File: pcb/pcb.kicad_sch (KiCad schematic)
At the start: 57 parts, among them IC1 TPS63802DLAT, IC2 TUSB320LIRWBR, J1 USB_C_Receptacle_PowerOnly_6P, J2 Soil_Sensor, J3 Pump, J4 Conn_01x03, Q1 2N7002, Q2 AO3401A, Q3 AO3400A, U1 BQ24075RGTR, U2 ESP-32S_USB-C_CH340_DevBoard

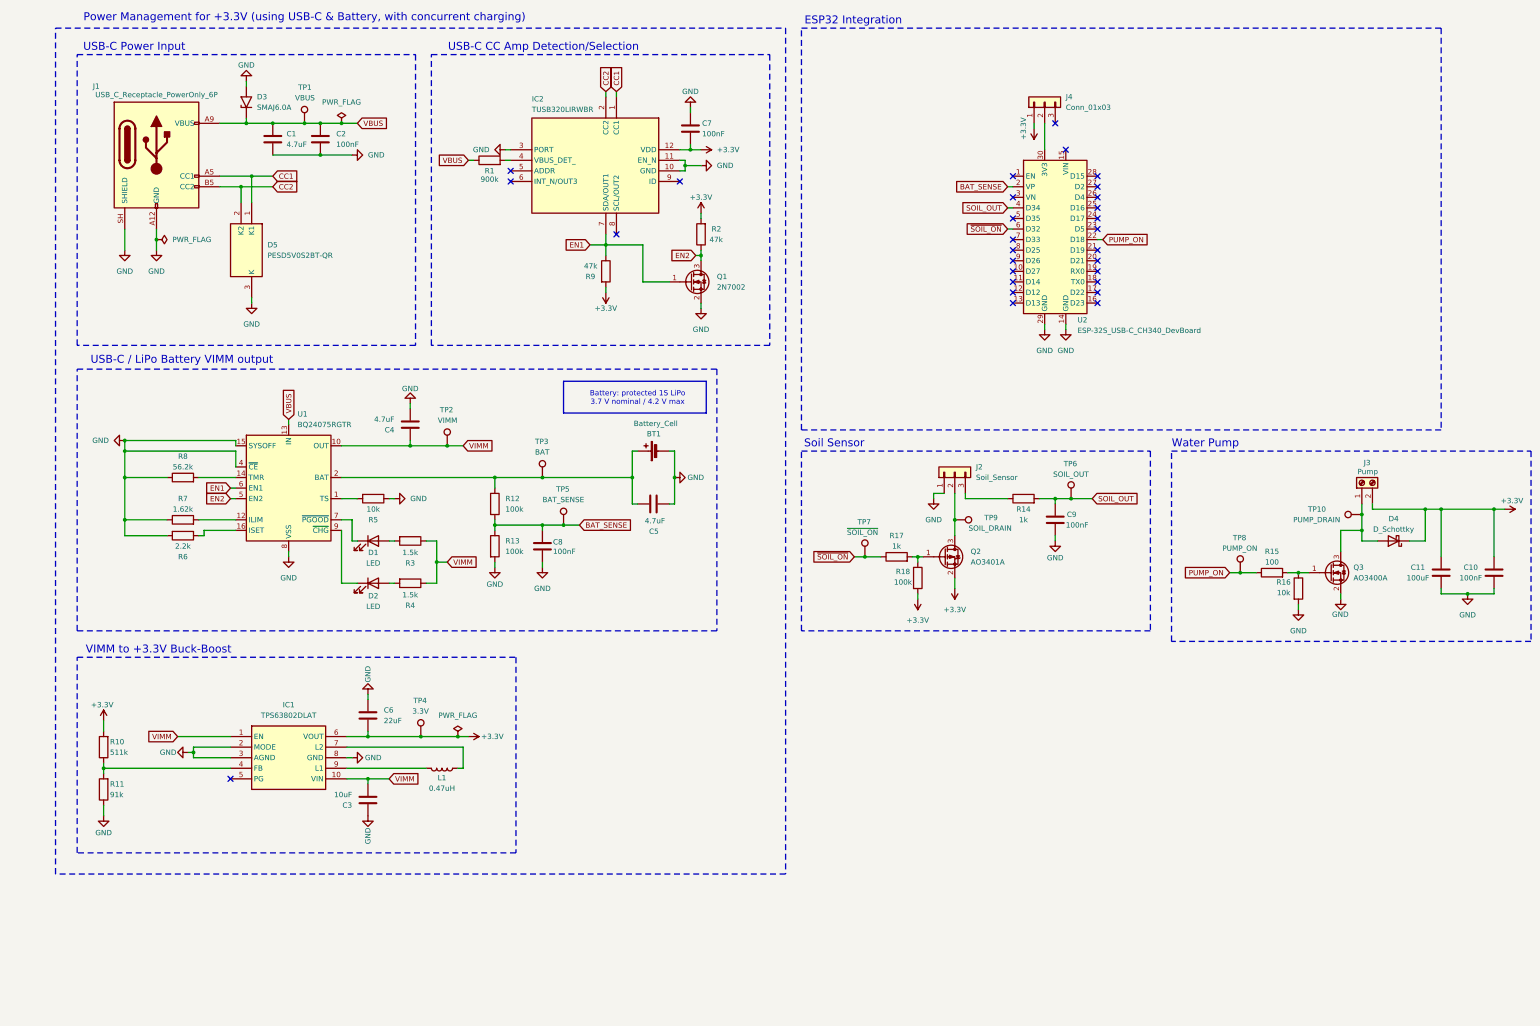
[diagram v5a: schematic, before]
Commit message: Added a new water level sensor
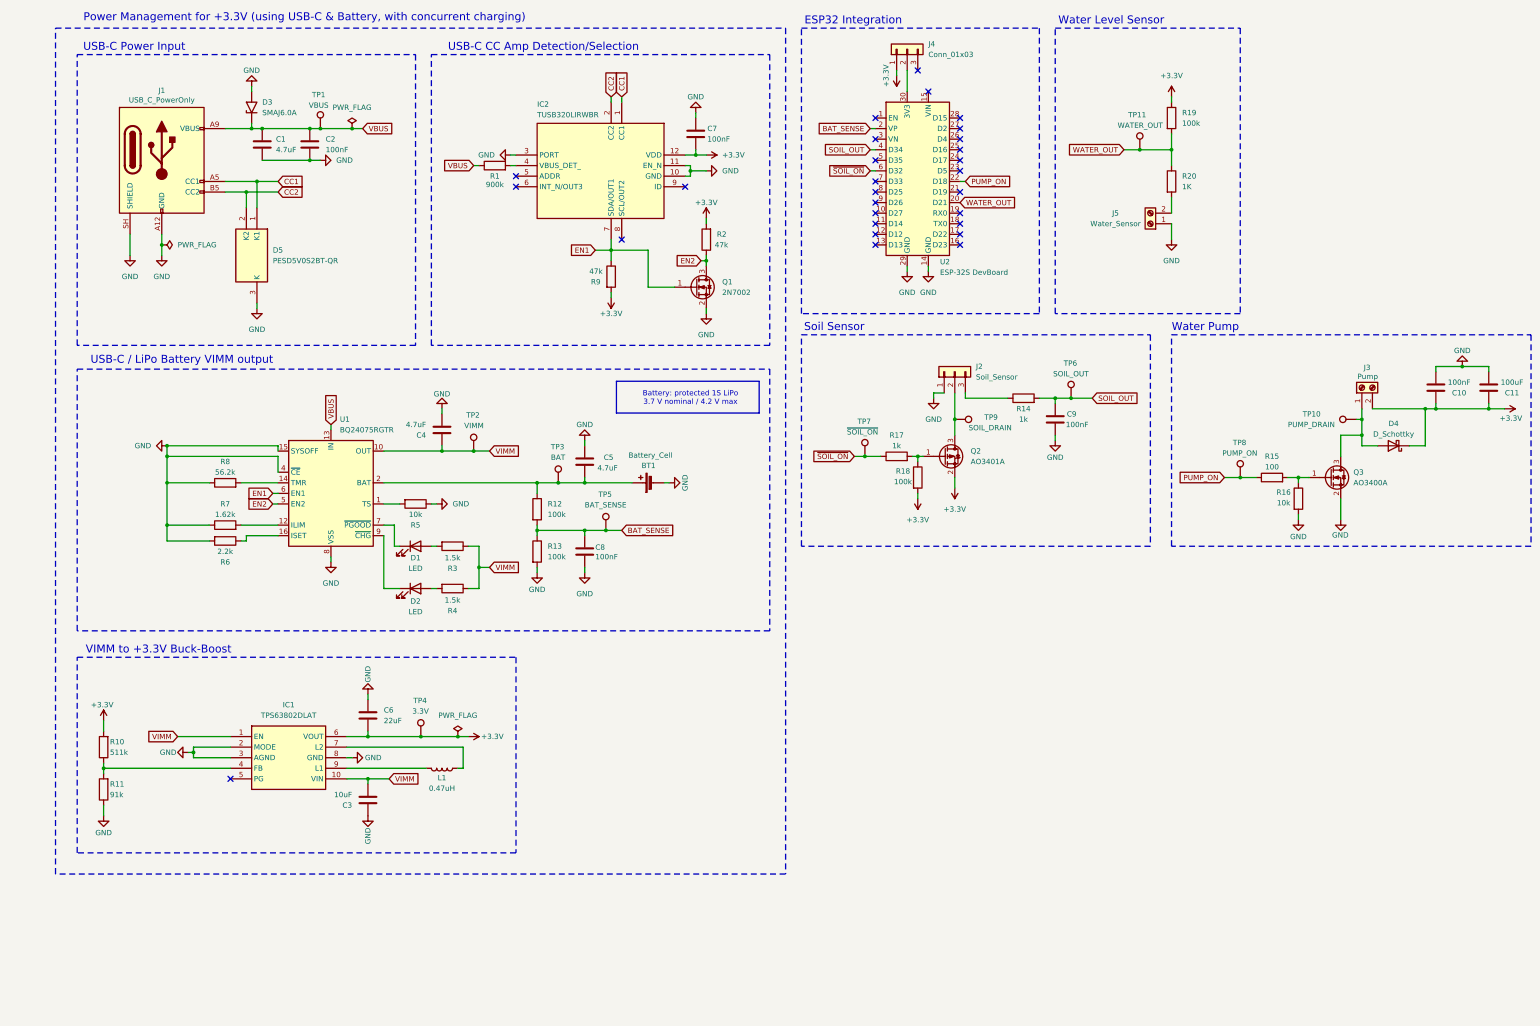
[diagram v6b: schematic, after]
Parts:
- added J5: Water_Sensor, TerminalBlock_Phoenix:TerminalBlock_Phoenix_MKDS-1,5-2-5.08_1x02_P5.08mm_Horizontal, symbol Connector:Screw_Terminal_01x02
- added R19: 100k, Resistor_SMD:R_1206_3216Metric_Pad1.30x1.75mm_HandSolder, symbol Device:R
- added R20: 1K, Resistor_SMD:R_1206_3216Metric_Pad1.30x1.75mm_HandSolder, symbol Device:R
- added TP11: WATER_OUT, TestPoint:TestPoint_Pad_D2.0mm, symbol Connector:TestPoint
- D5: footprint PESD5V0S2BTQR -> SamacSys:PESD5V0S2BTQR
- J1: value USB_C_Receptacle_PowerOnly_6P -> USB_C_PowerOnly
- U2: value ESP-32S_USB-C_CH340_DevBoard -> ESP-32S DevBoard
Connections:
- net +3.3V: now also R19.1
- net GND: now also J5.1 (Pin_1)
- net WATER_OUT: now reaches U2.20 (D21)
- net WATER_OUT: now also R19.2, R20.1, TP11.1
- new net: J5.2 (Pin_2), R20.2
- no-connect marks 29 -> 28
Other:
- note added: "Water Level Sensor"
- moved on the sheet: BT1, C1, C10, C11, C2, C4, C7, C8, C9, D1, D2, D3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

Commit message: Refactoring of the library location and startingt o use JLCPCB libraries for components
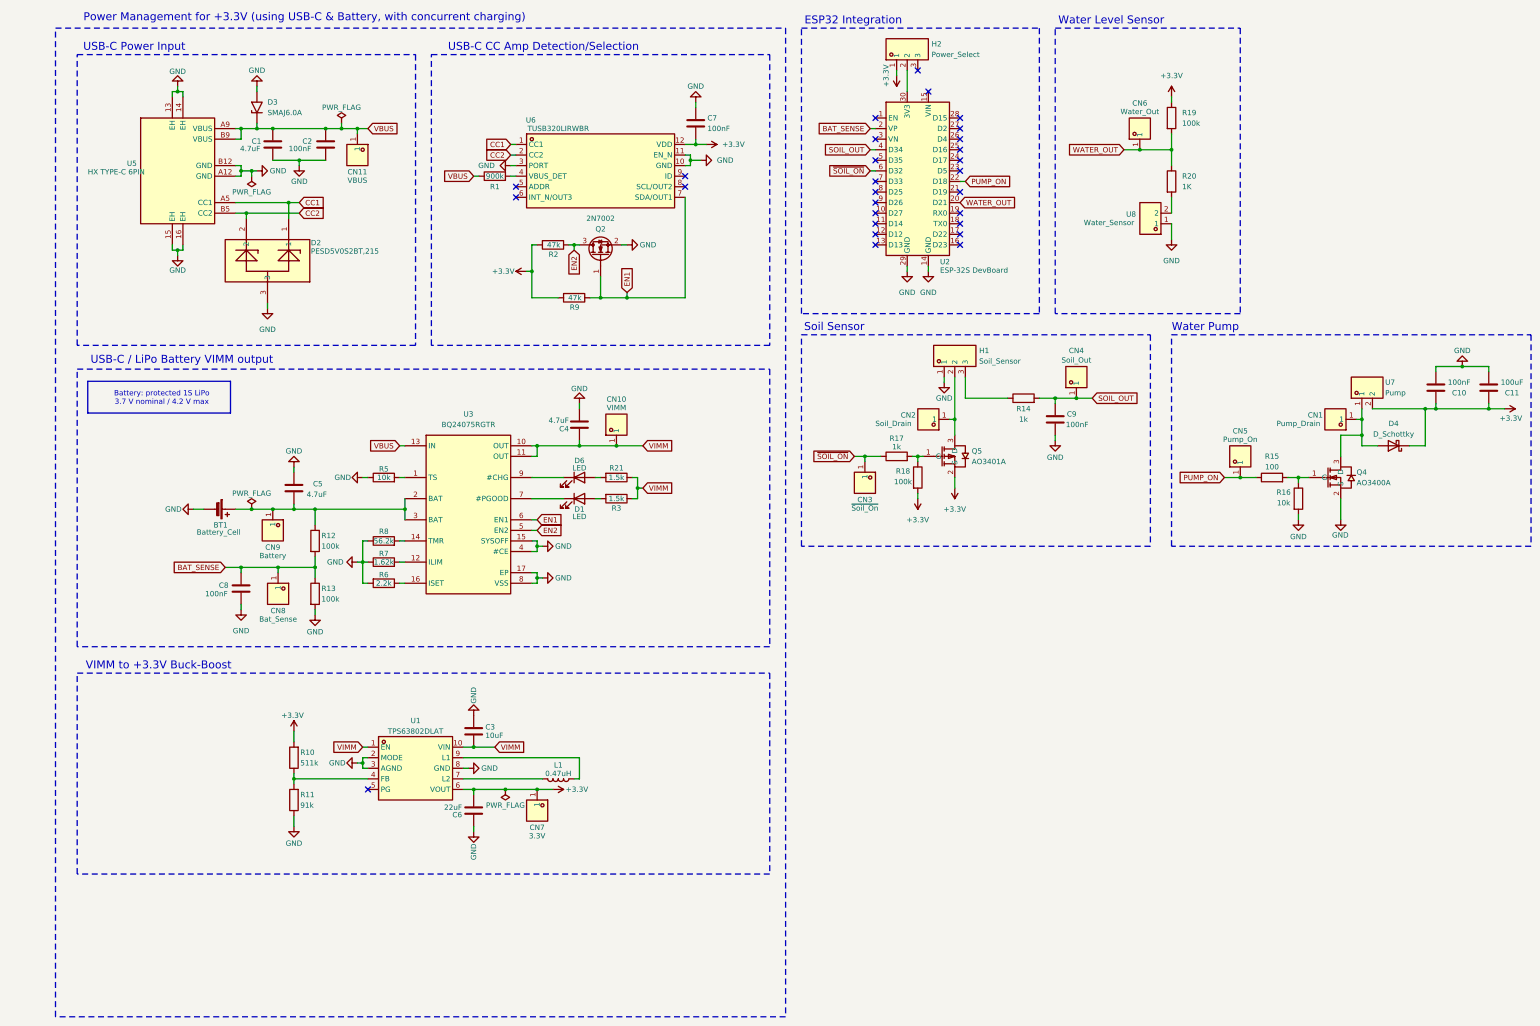
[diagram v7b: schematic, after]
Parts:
- removed D2: LED, LED_THT:LED_D4.0mm, symbol Device:LED
- removed D5: PESD5V0S2BT-QR, SamacSys:PESD5V0S2BTQR, symbol SamacSys:PESD5V0S2BT-QR
- removed IC1: TPS63802DLAT, SamacSys:TPS63802DLAT, symbol SamacSys:TPS63802DLAT
- removed IC2: TUSB320LIRWBR, SamacSys:TUSB320LIRWBR, symbol SamacSys:TUSB320LIRWBR
- removed J1: USB_C_PowerOnly, Connector_USB:USB_C_Receptacle_GCT_USB4125-xx-x-0190_6P_TopMnt_Horizontal, symbol Connector:USB_C_Receptacle_PowerOnly_6P
- removed J2: Soil_Sensor, Connector_PinHeader_2.54mm:PinHeader_1x03_P2.54mm_Vertical, symbol Connector_Generic:Conn_01x03
- removed J3: Pump, TerminalBlock_Phoenix:TerminalBlock_Phoenix_MKDS-1,5-2-5.08_1x02_P5.08mm_Horizontal, symbol Connector:Screw_Terminal_01x02
- removed J4: Conn_01x03, Connector_PinHeader_1.00mm:PinHeader_1x03_P1.00mm_Vertical, symbol Connector_Generic:Conn_01x03
- removed J5: Water_Sensor, TerminalBlock_Phoenix:TerminalBlock_Phoenix_MKDS-1,5-2-5.08_1x02_P5.08mm_Horizontal, symbol Connector:Screw_Terminal_01x02
- removed Q1: 2N7002, Package_TO_SOT_SMD:SOT-23, symbol Transistor_FET:2N7002
- removed Q2: AO3401A, Package_TO_SOT_SMD:SOT-23, symbol Transistor_FET:AO3401A
- removed Q3: AO3400A, Package_TO_SOT_SMD:SOT-23, symbol Transistor_FET:AO3400A
- removed R4: 1.5k, Resistor_SMD:R_1206_3216Metric_Pad1.30x1.75mm_HandSolder, symbol Device:R
- removed TP1: VBUS, TestPoint:TestPoint_Pad_D2.0mm, symbol Connector:TestPoint
- removed TP10: PUMP_DRAIN, TestPoint:TestPoint_Pad_D2.0mm, symbol Connector:TestPoint
- removed TP11: WATER_OUT, TestPoint:TestPoint_Pad_D2.0mm, symbol Connector:TestPoint
- removed TP2: VIMM, TestPoint:TestPoint_Pad_D2.0mm, symbol Connector:TestPoint
- removed TP3: BAT, TestPoint:TestPoint_Pad_D2.0mm, symbol Connector:TestPoint
- removed TP4: 3.3V, TestPoint:TestPoint_Pad_D2.0mm, symbol Connector:TestPoint
- removed TP5: BAT_SENSE, TestPoint:TestPoint_Pad_D2.0mm, symbol Connector:TestPoint
- removed TP6: SOIL_OUT, TestPoint:TestPoint_Pad_D2.0mm, symbol Connector:TestPoint
- removed TP7: ~{SOIL_ON}, TestPoint:TestPoint_Pad_D2.0mm, symbol Connector:TestPoint
- removed TP8: PUMP_ON, TestPoint:TestPoint_Pad_D2.0mm, symbol Connector:TestPoint
- removed TP9: SOIL_DRAIN, TestPoint:TestPoint_Pad_D2.0mm, symbol Connector:TestPoint
- removed U1: BQ24075RGTR, Package_DFN_QFN:VQFN-16-1EP_3x3mm_P0.5mm_EP1.6x1.6mm, symbol Battery_Management:BQ24075RGT
- added CN1: Pump_Drain, EasyEDA:TESTPOINT-SMD_L3.8-W2.0_RH-5019, symbol EasyEDA:RH-5019
- added CN10: VIMM, EasyEDA:TESTPOINT-SMD_L3.8-W2.0_RH-5019, symbol EasyEDA:RH-5019
- added CN11: VBUS, EasyEDA:TESTPOINT-SMD_L3.8-W2.0_RH-5019, symbol EasyEDA:RH-5019
- added CN2: Soil_Drain, EasyEDA:TESTPOINT-SMD_L3.8-W2.0_RH-5019, symbol EasyEDA:RH-5019
- added CN3: ~{Soil_On}, EasyEDA:TESTPOINT-SMD_L3.8-W2.0_RH-5019, symbol EasyEDA:RH-5019
- added CN4: Soil_Out, EasyEDA:TESTPOINT-SMD_L3.8-W2.0_RH-5019, symbol EasyEDA:RH-5019
- added CN5: Pump_On, EasyEDA:TESTPOINT-SMD_L3.8-W2.0_RH-5019, symbol EasyEDA:RH-5019
- added CN6: Water_Out, EasyEDA:TESTPOINT-SMD_L3.8-W2.0_RH-5019, symbol EasyEDA:RH-5019
- added CN7: 3.3V, EasyEDA:TESTPOINT-SMD_L3.8-W2.0_RH-5019, symbol EasyEDA:RH-5019
- added CN8: Bat_Sense, EasyEDA:TESTPOINT-SMD_L3.8-W2.0_RH-5019, symbol EasyEDA:RH-5019
- added CN9: Battery, EasyEDA:TESTPOINT-SMD_L3.8-W2.0_RH-5019, symbol EasyEDA:RH-5019
- added D2: PESD5V0S2BT,215, EasyEDA:SOT-23_L2.9-W1.3-P1.90-LS2.4-BR, symbol EasyEDA:PESD5V0S2BT,215
- added D6: LED, LED_THT:LED_D4.0mm, symbol Device:LED
- added H1: Soil_Sensor, EasyEDA:HDR-TH_3P-P2.54-V-M_PZ254V-11-03P, symbol EasyEDA:PZ254V-11-03P_C2937625
- added H2: Power_Select, EasyEDA:HDR-TH_3P-P2.54-V-M_PZ254V-11-03P, symbol EasyEDA:PZ254V-11-03P_C2937625
- added Q2: 2N7002, Package_TO_SOT_SMD:SOT-23, symbol Transistor_FET:2N7002
- added Q4: AO3400A, EasyEDA:SOT-23-3_L2.9-W1.3-P1.90-LS2.4-BR, symbol EasyEDA:AO3400A
- added Q5: AO3401A, EasyEDA:SOT-23_L2.9-W1.3-P1.90-LS2.4-BR, symbol EasyEDA:AO3401A
- added R21: 1.5k, Resistor_SMD:R_1206_3216Metric_Pad1.30x1.75mm_HandSolder, symbol Device:R
- added U1: TPS63802DLAT, EasyEDA:VSON-10-HR_L3.0-W2.0-P0.50-BL_TI_DLA, symbol EasyEDA:TPS63802DLAT
- added U3: BQ24075RGTR, EasyEDA:QFN-16_L3.0-W3.0-P0.50-TL-EP1.7, symbol EasyEDA:BQ24075RGTR
- added U5: HX TYPE-C 6PIN, EasyEDA:USB-C-SMD_HX-TYPE-C-6PIN, symbol EasyEDA:HXTYPE-C6PIN
- added U6: TUSB320LIRWBR, EasyEDA:X2QFN-12_L1.6-W1.6-P0.40-TL, symbol EasyEDA:TUSB320LIRWBR
- added U7: Pump, EasyEDA:CONN-TH_MX7620-7.62-02P-GN01-CU-S-A, symbol EasyEDA:MX7620-7.62-02P-GN01-CU-S-A
- added U8: Water_Sensor, EasyEDA:CONN-TH_MX7620-7.62-02P-GN01-CU-S-A, symbol EasyEDA:MX7620-7.62-02P-GN01-CU-S-A
- D3: footprint Diode_SMD:D_SMA_Handsoldering -> Diode_SMD:D_SMA
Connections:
- net +3.3V: now also CN7.1, H2.1, Q5.2 (S), U1.6 (VOUT), U6.12 (VDD), U7.2
- net BAT_SENSE: now also CN8.1
- net CC1: now also D2.1, U5.A5 (CC1), U6.1 (CC1)
- net CC2: now also D2.2, U5.B5 (CC2), U6.2 (CC2)
- net EN1: now also Q2.1 (G), U3.6 (EN1), U6.7 (SDA/OUT1)
- net EN2: now also Q2.3 (D), U3.5 (EN2)
- net GND: now also D2.3, H1.1, Q2.2 (S), Q4.2 (S), U1.2 (MODE), U1.3 (AGND), U1.8 (GND), U3.15 (SYSOFF), U3.17 (EP), U3.4 (#CE), U3.8 (VSS), U5.13 (EH), U5.14 (EH), U5.15 (EH), U5.16 (EH), U5.A12 (GND), U5.B12 (GND), U6.10 (GND), U6.11 (EN_N), U6.3 (PORT), U8.1
- net PUMP_ON: now also CN5.1
- net SOIL_OUT: now also CN4.1
- net VBUS: now also CN11.1, U3.13 (IN), U5.A9 (VBUS), U5.B9 (VBUS)
- net VIMM: now also CN10.1, R21.1, U1.1 (EN), U1.10 (VIN), U3.10 (OUT), U3.11 (OUT)
- net WATER_OUT: now also CN6.1
- net ~{SOIL_ON}: now also CN3.1
- net at D1.1 (K): now also U3.7 (#PGOOD)
- net at R14.1: now also H1.3
- net at BT1.1 (+), C5.1, R12.1: now also CN9.1, U3.2 (BAT), U3.3 (BAT)
- net at R20.2: now also U8.2
- net at L1.1: now also U1.9 (L1)
- net at L1.2: now also U1.7 (L2)
- net at R15.2, R16.1: now also Q4.1 (G)
- net at R1.2: now also U6.4 (VBUS_DET)
- net at D4.2 (A): now also CN1.1, Q4.3 (D), U7.1
- net at R17.2, R18.1: now also Q5.1 (G)
- net at R10.1, R11.2: now also U1.4 (FB)
- net at R5.2: now also U3.1 (TS)
- net at U2.30 (3V3): now also H2.2
- net at R8.2: now also U3.14 (TMR)
- net at R7.2: now also U3.12 (ILIM)
- net at R6.1: now also U3.16 (ISET)
- new net: CN2.1, H1.2, Q5.3 (D)
- new net: D6.1 (K), U3.9 (#CHG)
- new net: D6.2 (A), R21.2
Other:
- moved on the sheet: C3, C6, L1, R10, R11
